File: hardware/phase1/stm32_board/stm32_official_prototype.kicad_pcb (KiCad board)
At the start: 6 copper layers, 71 parts, among them CN14 USB_B_Micro, U1 STM32L496ZGTx, U13 USBLC6-2SC6, U8 TSV631AILT, U9 ESDALC6V1W5

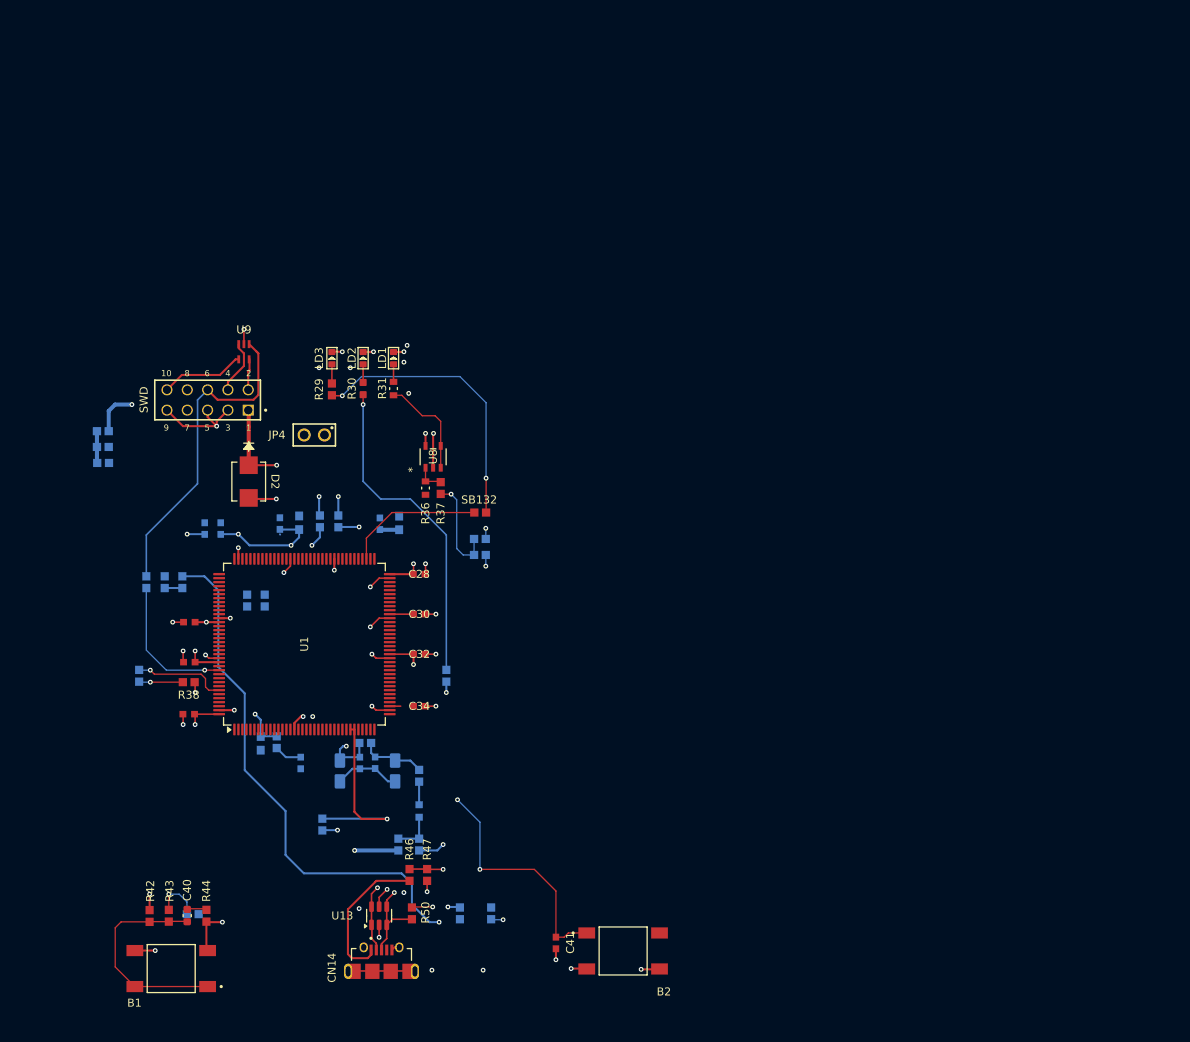
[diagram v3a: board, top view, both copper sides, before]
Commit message: stm32 PCB update - 70% finished (1.23.25)
- this board will definitely be ordered by next friday
- left off on completing routing within the signal layer (3)
- before i finalize i may need clarification on USB/power setup
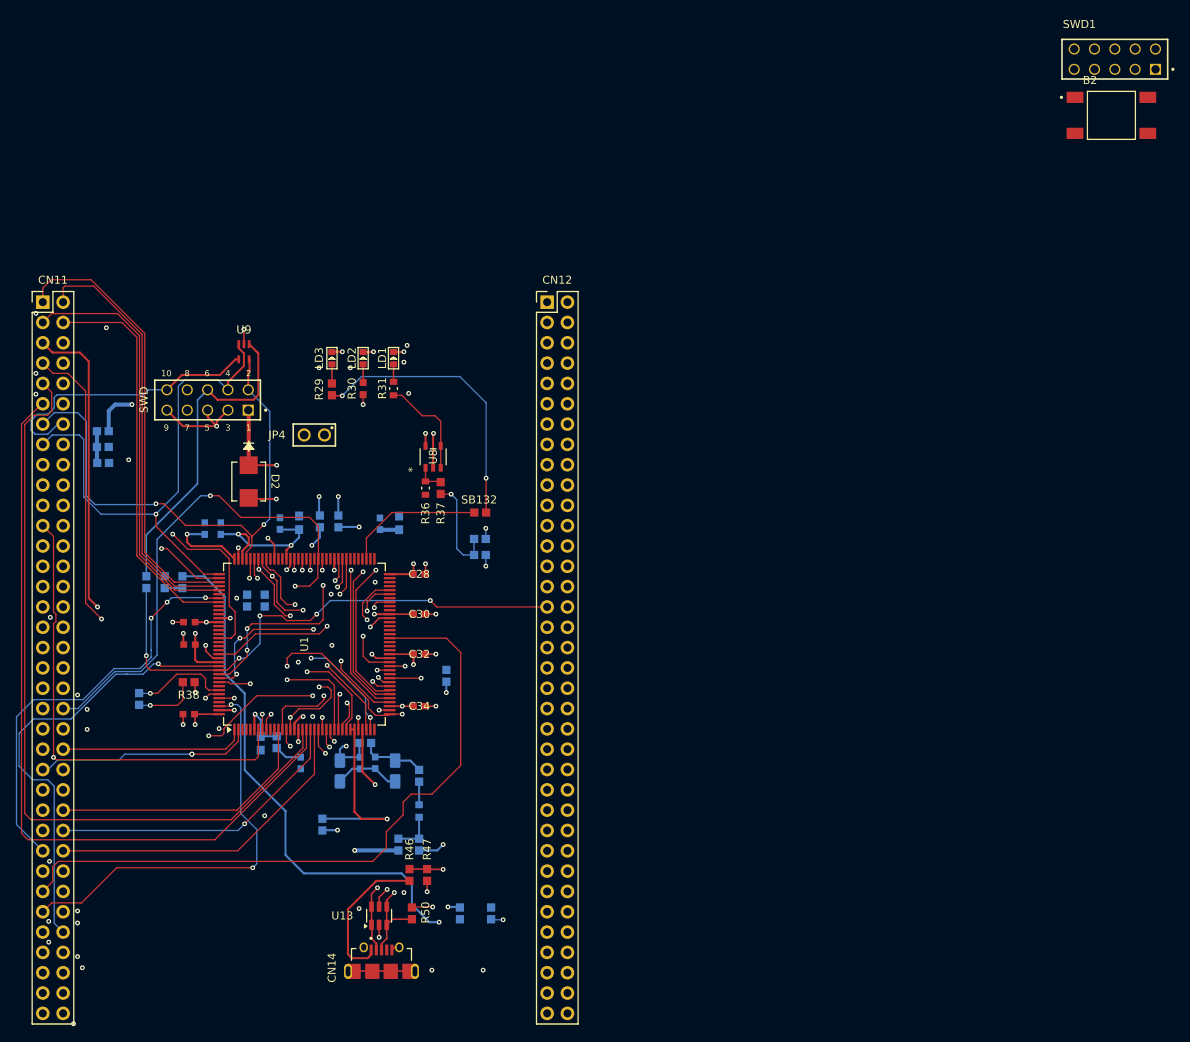
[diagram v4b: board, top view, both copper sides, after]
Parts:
- removed B1: TS02-66-60-BK-160-LCR-D, TS04_66_43_BK_260_SMT:SW_TS04-66-43-BK-260-SMT
- removed C40: C_0603_1608Metric, Capacitor_SMD:C_0603_1608Metric
- removed C41: 100nF, Capacitor,100nF,10%,16V,X7R,0603,YAGEO:CC0603N_YAG
- removed R42: 220K, RC0603FR-07220KL:RESC1607X60N
- removed R43: 330, RC0603FR-07330RL:RESC1607X60N
- removed R44: 100, RC0603FR-07100RL:RESC1607X60N
- removed SB197: Closed, RC0603JR-070RL:RESC1607X60N
- added CN11: Conn_02x36_Odd_Even, Connector_PinSocket_2.54mm:PinSocket_2x36_P2.54mm_Vertical, F.Cu at (113.5, 44.5)
- added CN12: Conn_02x36_Odd_Even, Connector_PinSocket_2.54mm:PinSocket_2x36_P2.54mm_Vertical, F.Cu at (176.9, 44.5)
- added SWD1: Conn_ARM_JTAG_SWD_10, SSW_105_06_G_D:SAMTEC_SSW-105-06-G-D, F.Cu at (249.5, 15.4)
- B2: value RESET -> TS02-66-60-BK-160-LCR-D
- moved B2 121.0 mm to (244.0, 21.1)
- moved SB171 2.90 mm to (122.5, 94.1)
- moved C31 2.20 mm to (128.8, 87.3)
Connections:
- B2 pad 1: GND -> VREF-
- B2 pad 4: GND -> VREF-
- C28 pad 2: GND -> VREF-
- C29 pad 2: GND -> VREF-
- C30 pad 2: GND -> VREF-
- C31 pad 2: GND -> VREF-
- C32 pad 2: GND -> VREF-
- C33 pad 2: GND -> VREF-
- C34 pad 2: GND -> VREF-
- C49 pad 2: GND -> VREF-
- C50 pad 2: GND -> VREF-
- C51 pad 2: GND -> VREF-
- C52 pad 2: GND -> VREF-
- C53 pad 2: GND -> VREF-
- C54 pad 2: GND -> VREF-
- C56 pad 2: GND -> VREF-
- C57 pad 2: GND -> VREF-
- C58 pad 2: GND -> VREF-
- C59 pad 2: GND -> VREF-
- C60 pad 2: GND -> VREF-
- C61 pad 2: GND -> VREF-
- CN14 pad 10: GND -> (no net)
- CN14 pad 5: GND -> VREF-
- CN14 pad 6: GND -> VREF-
- CN14 pad 7: GND -> (no net)
- CN14 pad 8: GND -> (no net)
- CN14 pad 9: GND -> (no net)
- D2 pad 2: GND -> VREF-
- LD1 pad -: GND -> (no net)
- LD2 pad -: GND -> (no net)
- LD3 pad -: GND -> (no net)
- R30 pad 1: Net-(R30-Pad1) -> PB7
- R36 pad 1: GND -> VREF-
- R38 pad 2: GND -> VREF-
- R47 pad 1: GND -> VREF-
- SB166 pad 1: GND -> VREF-
- SB166 pad 2: GND -> VREF-
- SB172 pad 2: Net-(R30-Pad1) -> PB7
- U1 pad 107: GND -> VREF-
- U1 pad 120: GND -> VREF-
- U1 pad 130: GND -> VREF-
- U1 pad 143: GND -> VREF-
- U1 pad 16: GND -> VREF-
- U1 pad 30: GND -> VREF-
- U1 pad 31: GND -> VREF-
- U1 pad 38: GND -> VREF-
- U1 pad 51: GND -> VREF-
- U1 pad 61: GND -> VREF-
- U1 pad 71: GND -> VREF-
- U1 pad 83: GND -> VREF-
- U1 pad 94: GND -> VREF-
- U13 pad 2: GND -> VREF-
- U8 pad 2: GND -> VREF-
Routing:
- net NRST: track 41.6 -> 163.8 mm, vias 2 -> 1
- net PF6: track 0.00 -> 98.5 mm
- net PF7: track 0.00 -> 97.9 mm
- net PG0: track 0.00 -> 85.7 mm
- net PA4: track 0.00 -> 79.8 mm, vias 0 -> 1
- net GND: track 89.4 -> 16.6 mm, vias 44 -> 20
- net VREF-: track 0.00 -> 66.2 mm, vias 0 -> 39
- net PG2: track 0.00 -> 62.7 mm, vias 0 -> 2
- net PA13: track 2.53 -> 64.8 mm, vias 0 -> 2
- net PC13: track 0.00 -> 59.0 mm, vias 0 -> 1
- net PA14: track 6.81 -> 65.8 mm, vias 0 -> 1
- net PG15: track 0.00 -> 57.1 mm, vias 0 -> 1
- net PC10: track 0.00 -> 55.9 mm
- net PA0: track 0.00 -> 53.9 mm, vias 0 -> 1
- net PC11: track 0.00 -> 53.0 mm
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
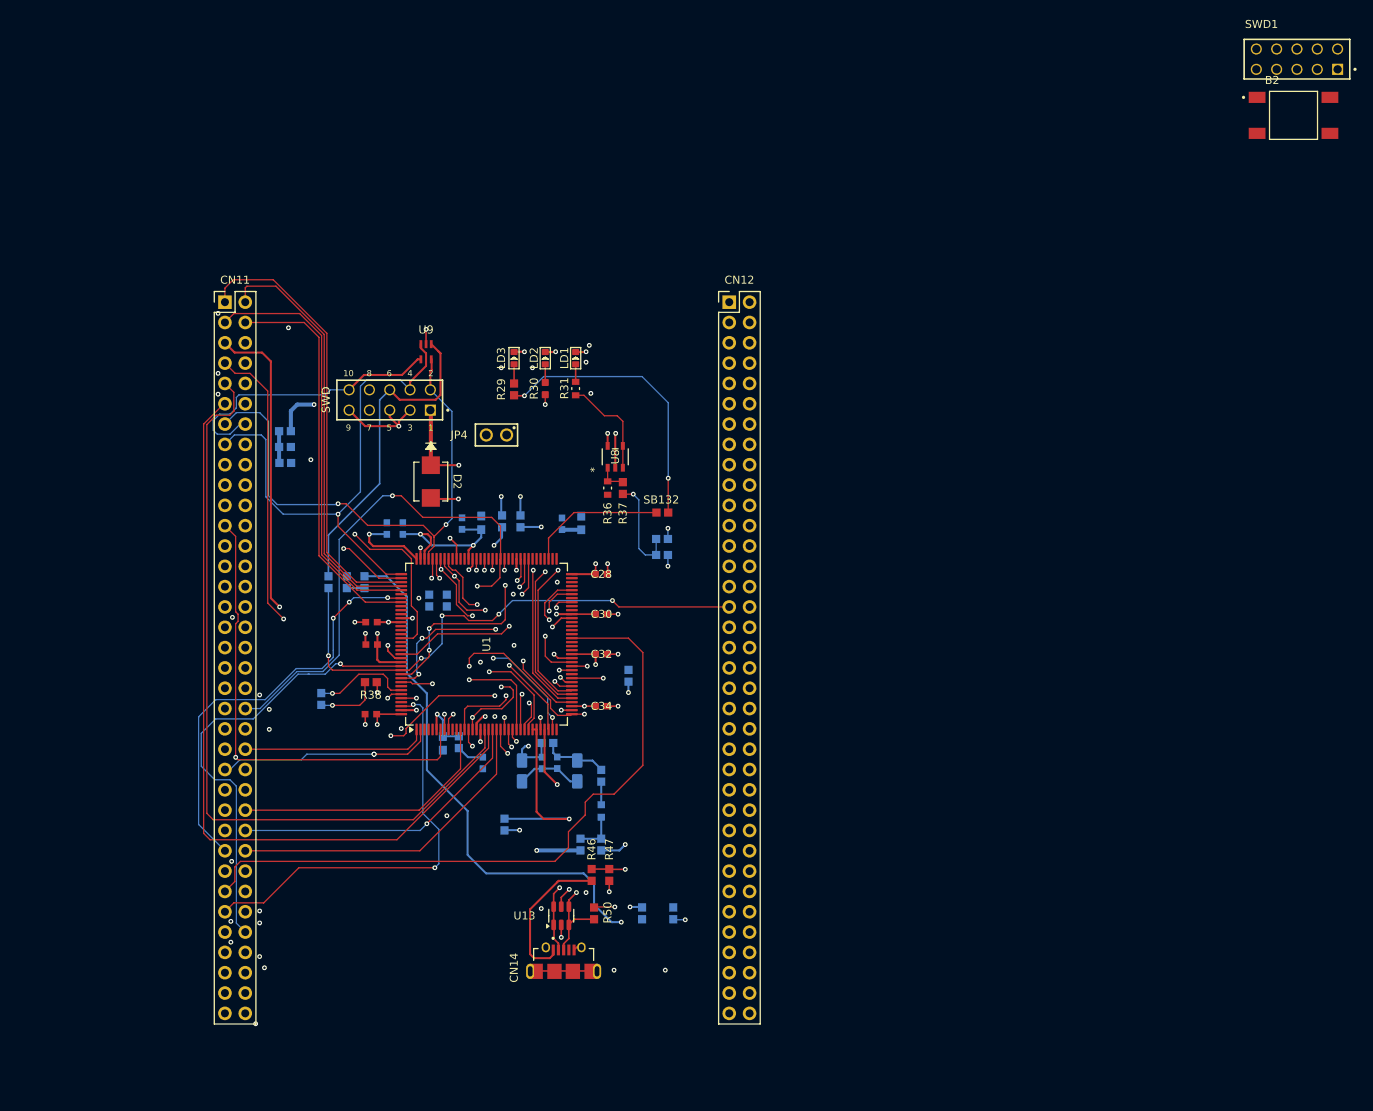
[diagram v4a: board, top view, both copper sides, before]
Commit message: STM32 board update (1.25.25)
- vastly improved the layout
- verified ALL footprints
- implemented correct JLCPCB design rules
- left off on labeling
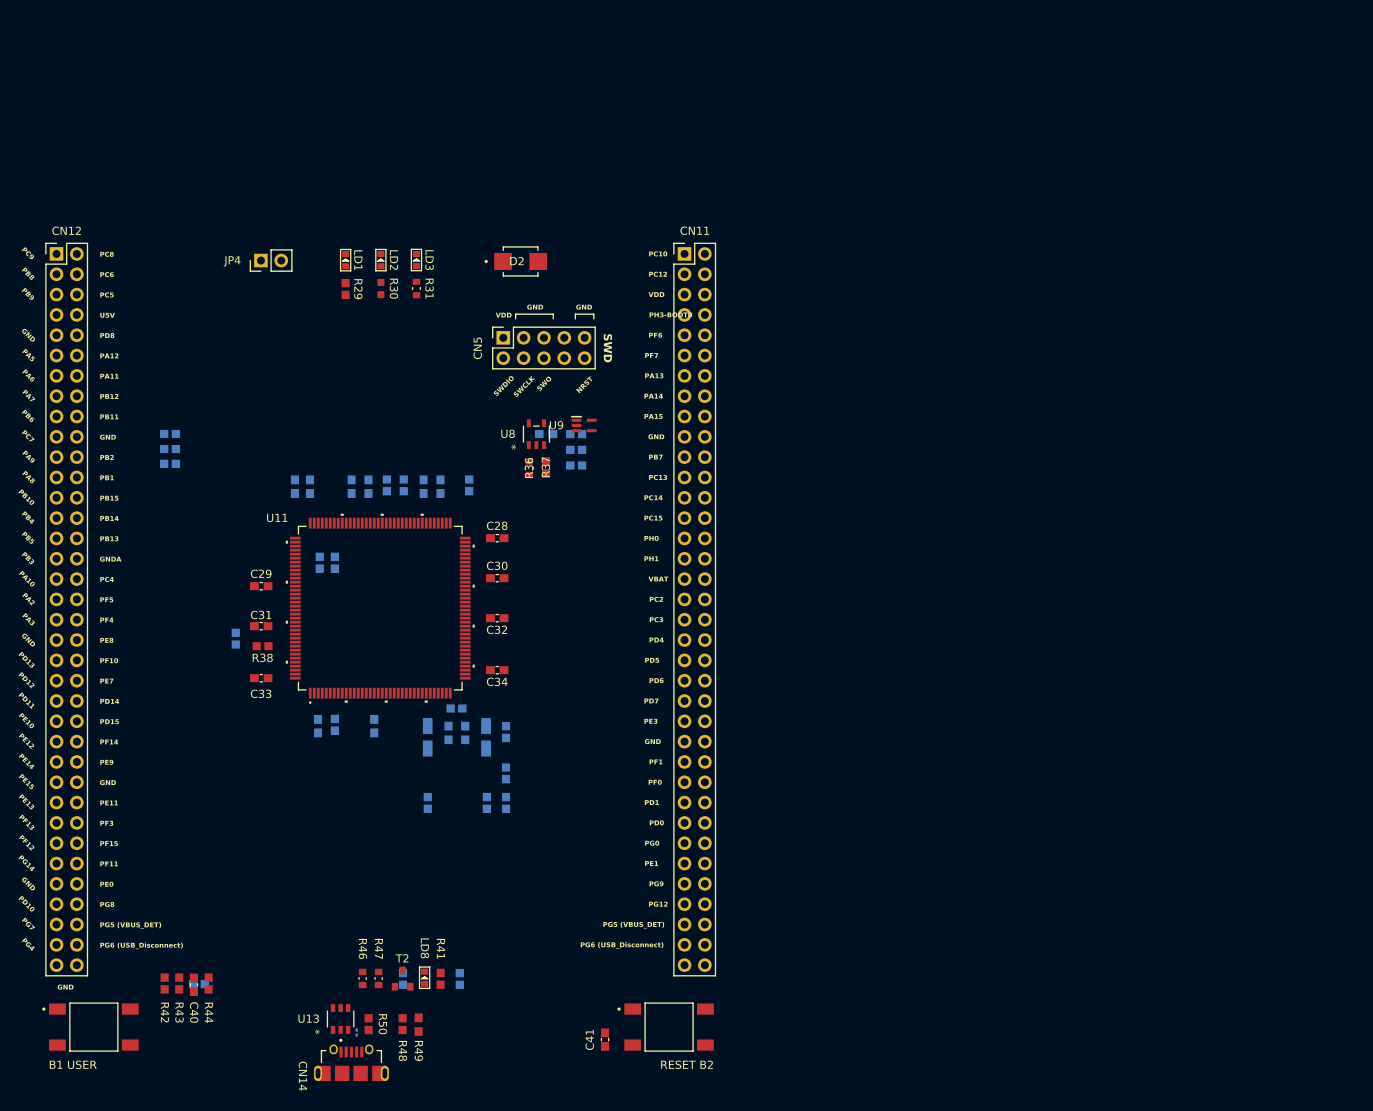
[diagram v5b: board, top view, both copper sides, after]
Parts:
- removed B2: TS02-66-60-BK-160-LCR-D, TS04_66_43_BK_260_SMT:SW_TS04-66-43-BK-260-SMT
- removed R54: 10K, RC0603FR-0710KL:RESC1607X60N
- removed SB135, SB162: RC0603JR-070RL, RC0603JR-070RL:RESC1607X60N
- removed SB171: Circuit Breaker-SMPS, RC0603JR-070RL:RESC1607X60N
- removed SWD, SWD1: Conn_ARM_JTAG_SWD_10, SSW_105_06_G_D:SAMTEC_SSW-105-06-G-D
- removed U1: STM32L496ZGTx, Package_QFP:LQFP-144_20x20mm_P0.5mm
- added B1 USER: TS02-66-60-BK-160-LCR-D, TS04_66_43_BK_260_SMT:SW_TS04-66-43-BK-260-SMT, F.Cu at (94.1, 135.1)
- added C40: [N/A], CC0603KRX7R7BB104:CAPC1608X90, F.Cu at (106.6, 129.8)
- added C41: 100nF, CC0603KRX7R7BB104:CAPC1608X90, F.Cu at (158.0, 136.7)
- added C45: [N/A], CC0603KRX7R7BB104:CAPC1608X90, B.Cu at (150.6, 61.0)
- added CN5: Conn_ARM_JTAG_SWD_10, Connector_PinSocket_2.54mm:PinSocket_2x05_P2.54mm_Vertical, F.Cu at (145.3, 49.0)
- added D6: ESDALC6V1-1U2, ESDALC6V1-1U2:DIODE_ESDALC6V1-1U2, B.Cu at (126.9, 135.8)
- added LD8: Green, SMD-LED-CLEAR-GREEN_0603_:LED-0603, F.Cu at (135.4, 128.9)
- added R41: 330, RC0603FR-07330RL:RESC1607X60N, F.Cu at (137.4, 129.1)
- added R42: 220K, RC0603FR-07220KL:RESC1607X60N, F.Cu at (102.9, 129.7)
- added R43: 330, RC0603FR-07330RL:RESC1607X60N, F.Cu at (104.7, 129.7)
- added R44: 100, RC0603FR-07100RL:RESC1607X60N, F.Cu at (108.4, 129.7)
- added R48: 22K, RC0603FR-0722KL:RESC1607X60N, F.Cu at (132.7, 134.8)
- added R49: 47K, RC0603FR-0747KL:RESC1608X55, F.Cu at (134.7, 134.8)
- added RESET B2: TS02-66-60-BK-160-LCR-D, TS04_66_43_BK_260_SMT:SW_TS04-66-43-BK-260-SMT, F.Cu at (166.0, 135.1)
- added SB119: Open, RC0603JR-070RL:RESC1607X60N, B.Cu at (154.4, 61.0)
- added SB197: Closed, RC0603JR-070RL:RESC1607X60N, B.Cu at (107.2, 129.7)
- added T2: 9013, MMBT9013:SOT-23, F.Cu at (132.7, 129.1)
- added U11: STM32L496ZGTx, STM32L496ZGT6:LQFP144-20x20mm_STM, F.Cu at (129.9, 82.8)
- C28, C29, C30, C31, C32, C33, C34, C49, C50, C51, C53, C57, C58, C61: footprint Capacitor,100nF,10%,16V,X7R,0603,YAGEO:CC0603N_YAG -> CC0603KRX7R7BB104:CAPC1608X90
- C52, C54: footprint Capacitor，4.7uF，16V， X5R，10%，0603:CAPC1608X90 -> CC0603KRX5R7BB475:CAPC1608X90
- C56, C59: footprint TAN Capacitor,1uF,10%,16V,A Type,AVX:CAPMP3216X180N -> TAJA105K016R:CAPMP3216X166
- C60: footprint Capacitor,1uF,0603,16V,10%,X5R,YAGEO:CAPC1608X90 -> CC0603KRX5R7BB105:CAPC1608X90
- D2: footprint SMLVT3V3:SMB_STM -> SMLVT3V3:DIOM4336X265N
- JP4: value Conn_02x01 -> Conn_01x02_Pin; footprint HDR_1x2_2R54:61300211121 -> Connector_PinHeader_2.54mm:PinHeader_1x02_P2.54mm_Vertical
- L3: footprint FERRITEBEAD_0603:CAPC1608X90N -> FCM1608KF-601T05:FB0603
- R30: footprint RES-680R-0603_:R0603 -> SMD-RES-680R-1_-1_10W_0603_:R0603
- R46: footprint RC0603FR-071K5L:RESC1607X60N -> RC0603FR-07430KL:RESC1608X55N
- R47: footprint RC0603FR-071K5L:RESC1607X60N -> RC0603FR-07620KL:RESC1608X55N
- SB132: moved to B.Cu
- SB172, SB199, SB201: value RC0603JR-070RL -> Closed
- U13: footprint Package_TO_SOT_SMD:SOT-23-6 -> USBLC6_2SC6:SOT23-6L_STM
- U9: footprint ESDALC6V1W5 (1):SOT323-5L -> ESDALC6V1W5:SOT65P210X110-5N
- moved CN12 84.3 mm to (92.8, 38.5)
- moved CN11 57.8 mm to (170.9, 38.5)
- moved SB172 49.3 mm to (111.8, 86.6)
- moved JP4 36.6 mm to (115.0, 39.3), turned to 90 degrees
- moved R47 31.6 mm to (129.7, 129.0)
- moved R46 31.4 mm to (127.7, 129.0)
- moved R50 31.4 mm to (128.4, 134.8)
- moved LD1 31.2 mm to (125.6, 39.3)
- moved SB199 31.0 mm to (132.7, 129.1)
- moved U13 30.4 mm to (124.9, 134.1)
- moved D2 29.7 mm to (147.4, 39.4), turned to 0 degrees
- moved CN14 29.4 mm to (126.3, 141.3)
- moved SB201 27.9 mm to (139.8, 129.1)
- moved R29 24.5 mm to (125.6, 42.9)
- moved SB132 24.4 mm to (141.0, 67.4), turned to 90 degrees
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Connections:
- net PG6 renamed PG6 (USB_Disconnect)
- C28 pad 2: VREF- -> GND
- C29 pad 2: VREF- -> GND
- C30 pad 2: VREF- -> GND
- C31 pad 2: VREF- -> GND
- C32 pad 2: VREF- -> GND
- C33 pad 2: VREF- -> GND
- C34 pad 2: VREF- -> GND
- C49 pad 2: VREF- -> GND
- C50 pad 2: VREF- -> GND
- C51 pad 2: VREF- -> GND
- C52 pad 2: VREF- -> GND
- C53 pad 2: VREF- -> GND
- C54 pad 2: VREF- -> GND
- C56 pad 2: VREF- -> GNDA
- C57 pad 2: VREF- -> GNDA
- C58 pad 2: VREF- -> GNDA
- C59 pad 2: VREF- -> GNDA
- C60 pad 2: VREF- -> GND
- C61 pad 2: VREF- -> GND
- CN11 pad 19: VREF- -> GND
- CN11 pad 20: VREF- -> GND
- CN11 pad 22: VREF- -> GND
- CN11 pad 49: VREF- -> GND
- CN11 pad 60: VREF- -> GND
- CN11 pad 71: VREF- -> GND
- CN11 pad 72: VREF- -> GND
- CN11 pad 8: VREF- -> GND
- CN12 pad 20: VREF- -> GND
- CN12 pad 32: VREF- -> GNDA
- CN12 pad 39: VREF- -> GND
- CN12 pad 54: VREF- -> GND
- CN12 pad 63: VREF- -> GND
- CN12 pad 68: PG5 -> PG5 (VBUS_DET)
- CN12 pad 7: VREF+ -> Net-(CN12-Pin_7)
- CN12 pad 71: VREF- -> GND
- CN12 pad 72: VREF- -> GND
- CN12 pad 9: VREF- -> GND
- CN14 pad 1: USB_VBUS -> PA9
- CN14 pad 2: PA11 -> USB_DM
- CN14 pad 3: PA12 -> USB_DP
- CN14 pad 4: unconnected-(CN14-ID-Pad4) -> PA10
- CN14 pad 5: VREF- -> GND
- D2 pad 2: VREF- -> GND
- JP4 pad 1: PG5 -> PG5 (VBUS_DET)
- JP4 pad 2: USB_GPIO_IN -> VBUS_DET
- R30 pad 1: PB7 -> Net-(R30-Pad1)
- R36 pad 1: VREF- -> GND
- R38 pad 2: VREF- -> GND
- R46 pad 1: USB_VBUS -> PA9
- R47 pad 1: VREF- -> GND
- R50 pad 1: PA12 -> USB_DP
- SB142 pad 2: PA11 -> USB_DM
- SB143 pad 2: PA12 -> USB_DP
- SB166 pad 1: VREF- -> GND
- SB166 pad 2: VREF- -> GNDA
- SB172 pad 2: PB7 -> Net-(R30-Pad1)
- SB199 pad 1: PG5 -> VBUS_DET
- U13 pad 1: PA11 -> USB_DM
- U13 pad 2: VREF- -> GND
- U13 pad 3: PA12 -> USB_DP
- U13 pad 4: PA12 -> USB_DP
- U13 pad 5: USB_VBUS -> PA9
- U13 pad 6: PA11 -> USB_DM
- U8 pad 2: VREF- -> GND
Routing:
- net NRST: track 163.8 -> 0.00 mm, vias 1 -> 0
- net PB3: track 107.3 -> 0.00 mm, vias 5 -> 0
- net PF6: track 98.5 -> 0.00 mm
- net PF7: track 97.9 -> 0.00 mm
- net USB_VBUS: track 87.5 -> 0.00 mm, vias 2 -> 0
- net PG0: track 85.7 -> 0.00 mm
- net PA4: track 79.8 -> 0.00 mm, vias 1 -> 0
- net VDD: track 75.5 -> 0.00 mm, vias 6 -> 0
- net VREF-: track 66.2 -> 0.00 mm, vias 39 -> 0
- net PA14: track 65.8 -> 0.00 mm, vias 1 -> 0
- net PA13: track 64.8 -> 0.00 mm, vias 2 -> 0
- net PG2: track 62.7 -> 0.00 mm, vias 2 -> 0
- net PC13: track 59.0 -> 0.00 mm, vias 1 -> 0
- net PG15: track 57.1 -> 0.00 mm, vias 1 -> 0
- net PC10: track 55.9 -> 0.00 mm
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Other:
- board text added: "GND"
- board text added: "GNDA"
- board text added: "NRST"
- board text added: "PA10"
- board text added: "PA11"
- board text added: "PA12"
- board text added: "PA13"
- board text added: "PA14"
- board text added: "PA15"
- board text added: "PA2"
- board text added: "PA3"
- board text added: "PA5"
- board text added: "PA6"
- board text added: "PA7"
- board text added: "PA8"
- board text added: "PA9"
- board text added: "PB1"
- board text added: "PB10"
- board text added: "PB11"
- board text added: "PB12"
- board text added: "PB13"
- board text added: "PB14"
- board text added: "PB15"
- board text added: "PB2"
- board text added: "PB3"
- board text added: "PB4"
- board text added: "PB5"
- board text added: "PB6"
- board text added: "PB7"
- board text added: "PB8"
- board text added: "PB9"
- board text added: "PC10"
- board text added: "PC12"
- board text added: "PC13"
- board text added: "PC14"
- board text added: "PC15"
- board text added: "PC2"
- board text added: "PC3"
- board text added: "PC4"
- board text added: "PC5"
- board text added: "PC6"
- board text added: "PC7"
- board text added: "PC8"
- board text added: "PC9"
- board text added: "PD0"
- board text added: "PD1"
- board text added: "PD10"
- board text added: "PD11"
- board text added: "PD12"
- board text added: "PD13"
- board text added: "PD14"
- board text added: "PD15"
- board text added: "PD4"
- board text added: "PD5"
- board text added: "PD6"
- board text added: "PD7"
- board text added: "PD8"
- board text added: "PE0"
- board text added: "PE1"
- board text added: "PE10"
- board text added: "PE11"
- board text added: "PE12"
- board text added: "PE13"
- board text added: "PE14"
- board text added: "PE15"
- board text added: "PE3"
- board text added: "PE7"
- board text added: "PE8"
- board text added: "PE9"
- board text added: "PF0"
- board text added: "PF1"
- board text added: "PF10"
- board text added: "PF11"
- board text added: "PF12"
- board text added: "PF13"
- board text added: "PF14"
- board text added: "PF15"
- board text added: "PF3"
- board text added: "PF4"
- board text added: "PF5"
- board text added: "PF6"
- board text added: "PF7"
- board text added: "PG0"
- board text added: "PG12"
- board text added: "PG14"
- board text added: "PG4"
- board text added: "PG5 (VBUS_DET)"
- board text added: "PG6 (USB_Disconnect)"
- board text added: "PG7"
- board text added: "PG8"
- board text added: "PG9"
- board text added: "PH0"
- board text added: "PH1"
- board text added: "PH3-BOOT0"
- board text added: "SWCLK"
- board text added: "SWD"
- board text added: "SWDIO"
- board text added: "SWO"
- board text added: "U5V"
- board text added: "VBAT"
- board text added: "VDD"
- board text removed: "1"
- board text removed: "10"
- board text removed: "2"
- board text removed: "3"
- board text removed: "4"
- board text removed: "5"
- board text removed: "6"
- board text removed: "7"
- board text removed: "8"
- board text removed: "9"
